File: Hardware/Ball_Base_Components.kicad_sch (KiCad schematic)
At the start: 7 parts, among them U1 TL072

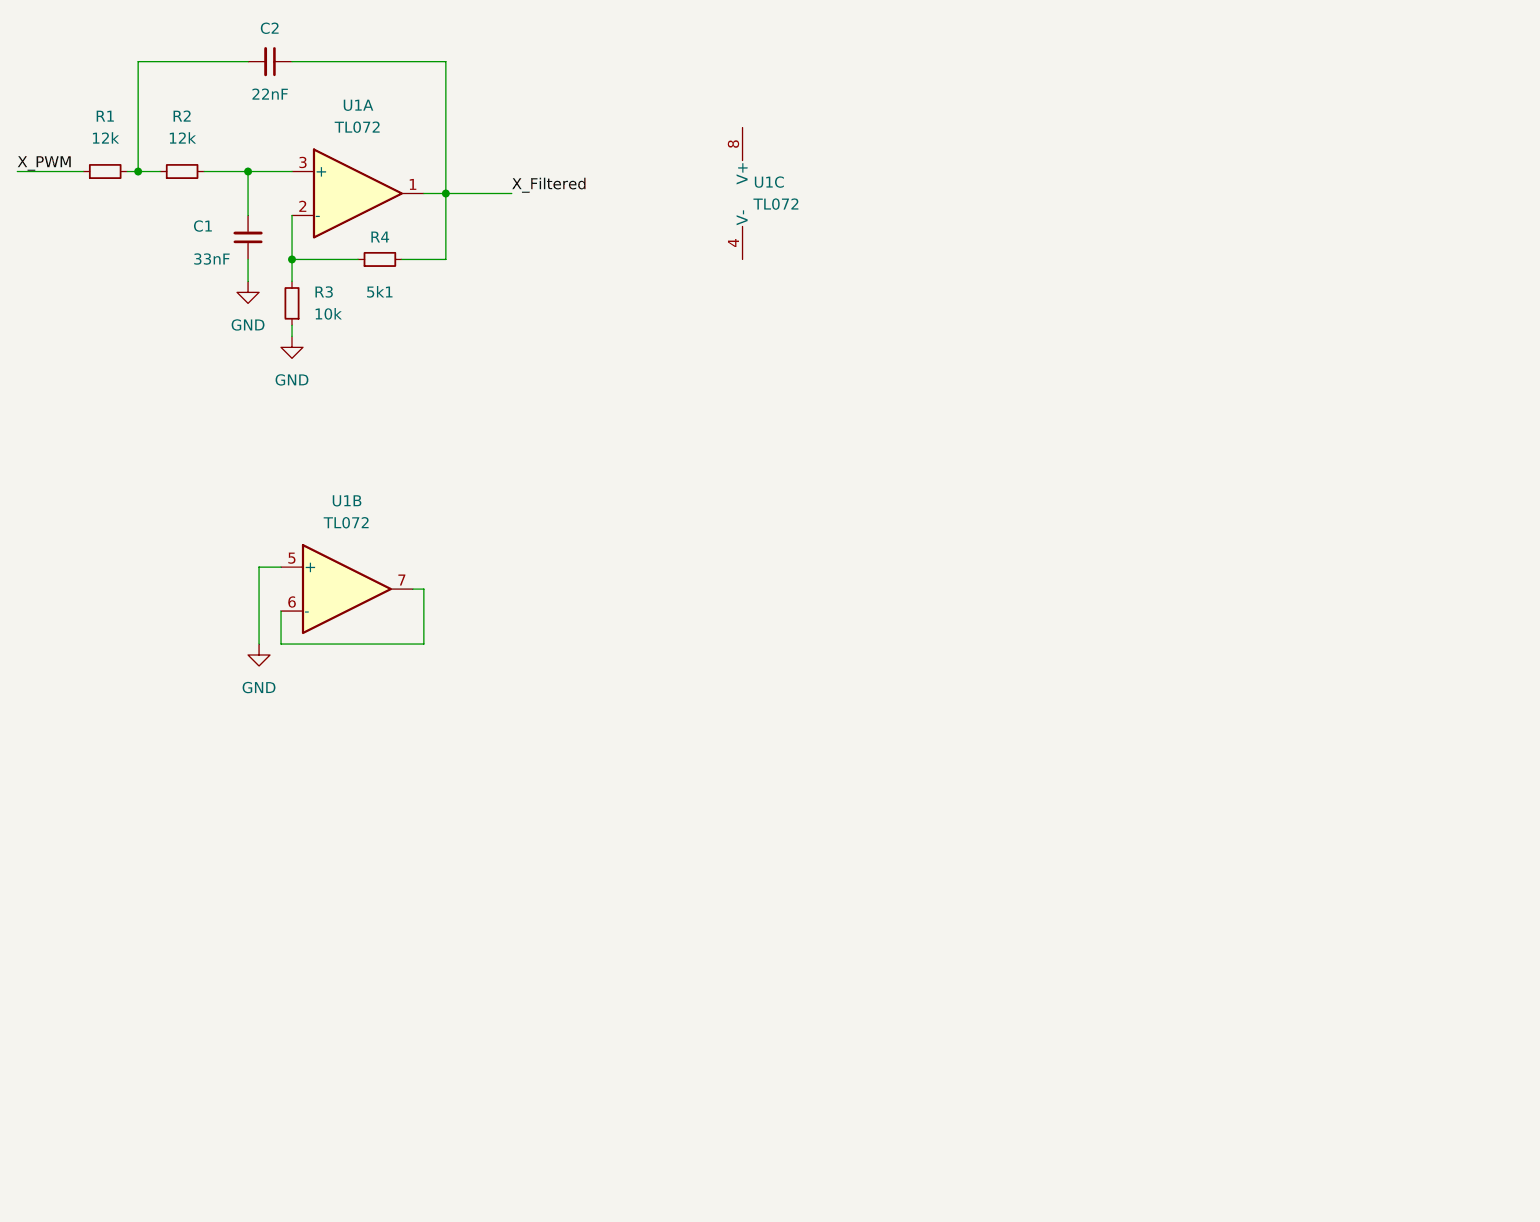
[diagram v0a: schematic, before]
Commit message: Updated base unit to support 3 channels of HID to PWM
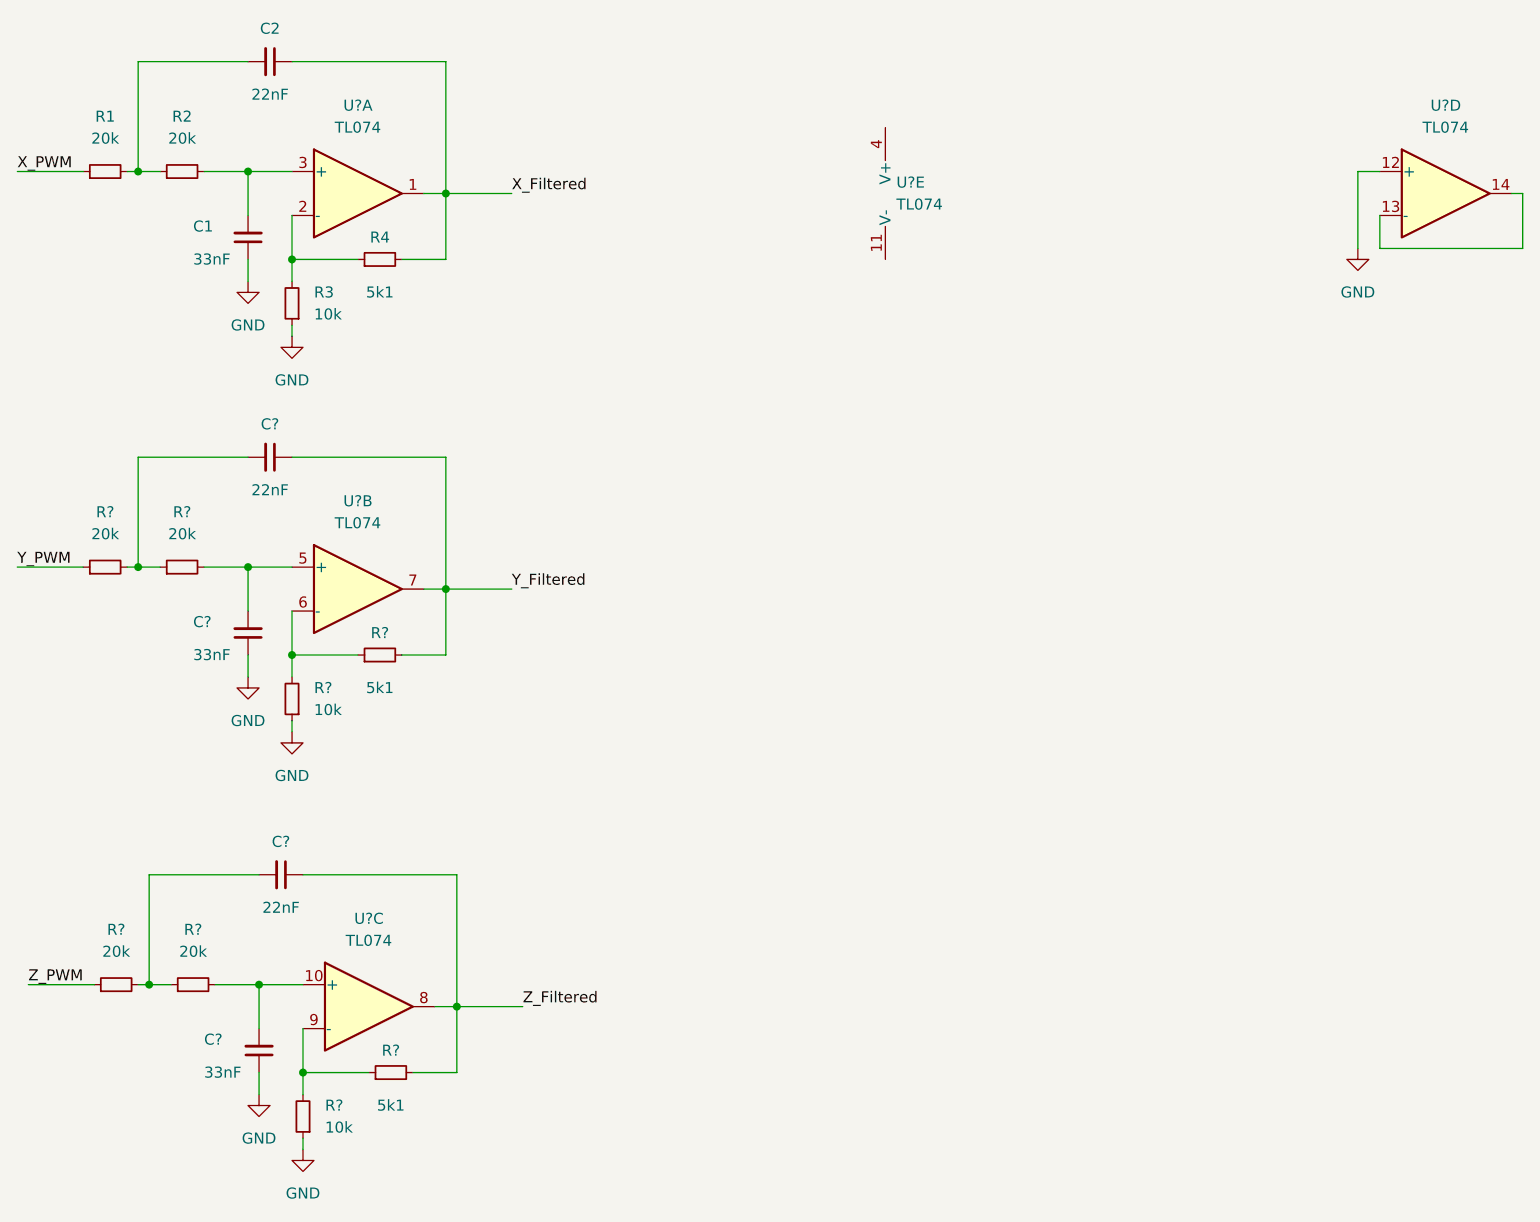
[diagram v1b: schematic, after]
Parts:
- removed U1: TL072, symbol Amplifier_Operational:TL072
- added C? (x2): 33nF, symbol Device:C_Small
- added C? (x2): 22nF, symbol Device:C_Small
- added R? (x4): 20k, symbol Device:R_Small
- added R? (x2): 5k1, symbol Device:R_Small
- added R? (x2): 10k, symbol Device:R_Small
- added U? (x5): TL074, symbol Amplifier_Operational:TL074
- R1, R2: value 12k -> 20k
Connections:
- net GND: now also C?.1, C?.1, R?.1, R?.1, U?.12 (+)
- net X_Filtered: now also U?.1
- net at R3.2, R4.1: now also U?.2 (-)
- net at C1.2, R2.2: now also U?.3 (+)
- new net: C?.2, R?.1, R?.2 (x2)
- new net: C?.2, R?.2, U?.5 (+)
- new net: C?.2, R?.2, U?.10 (+)
- new net: R?.1, R?.2, U?.9 (-)
- new net: U?.13 (-), U?.14
- new net: R?.1, R?.2, U?.6 (-)
- new net Y_Filtered: C?.1, R?.2, U?.7
- new net Y_PWM: R?.1
- new net Z_Filtered: C?.1, R?.2, U?.8
- new net Z_PWM: R?.1

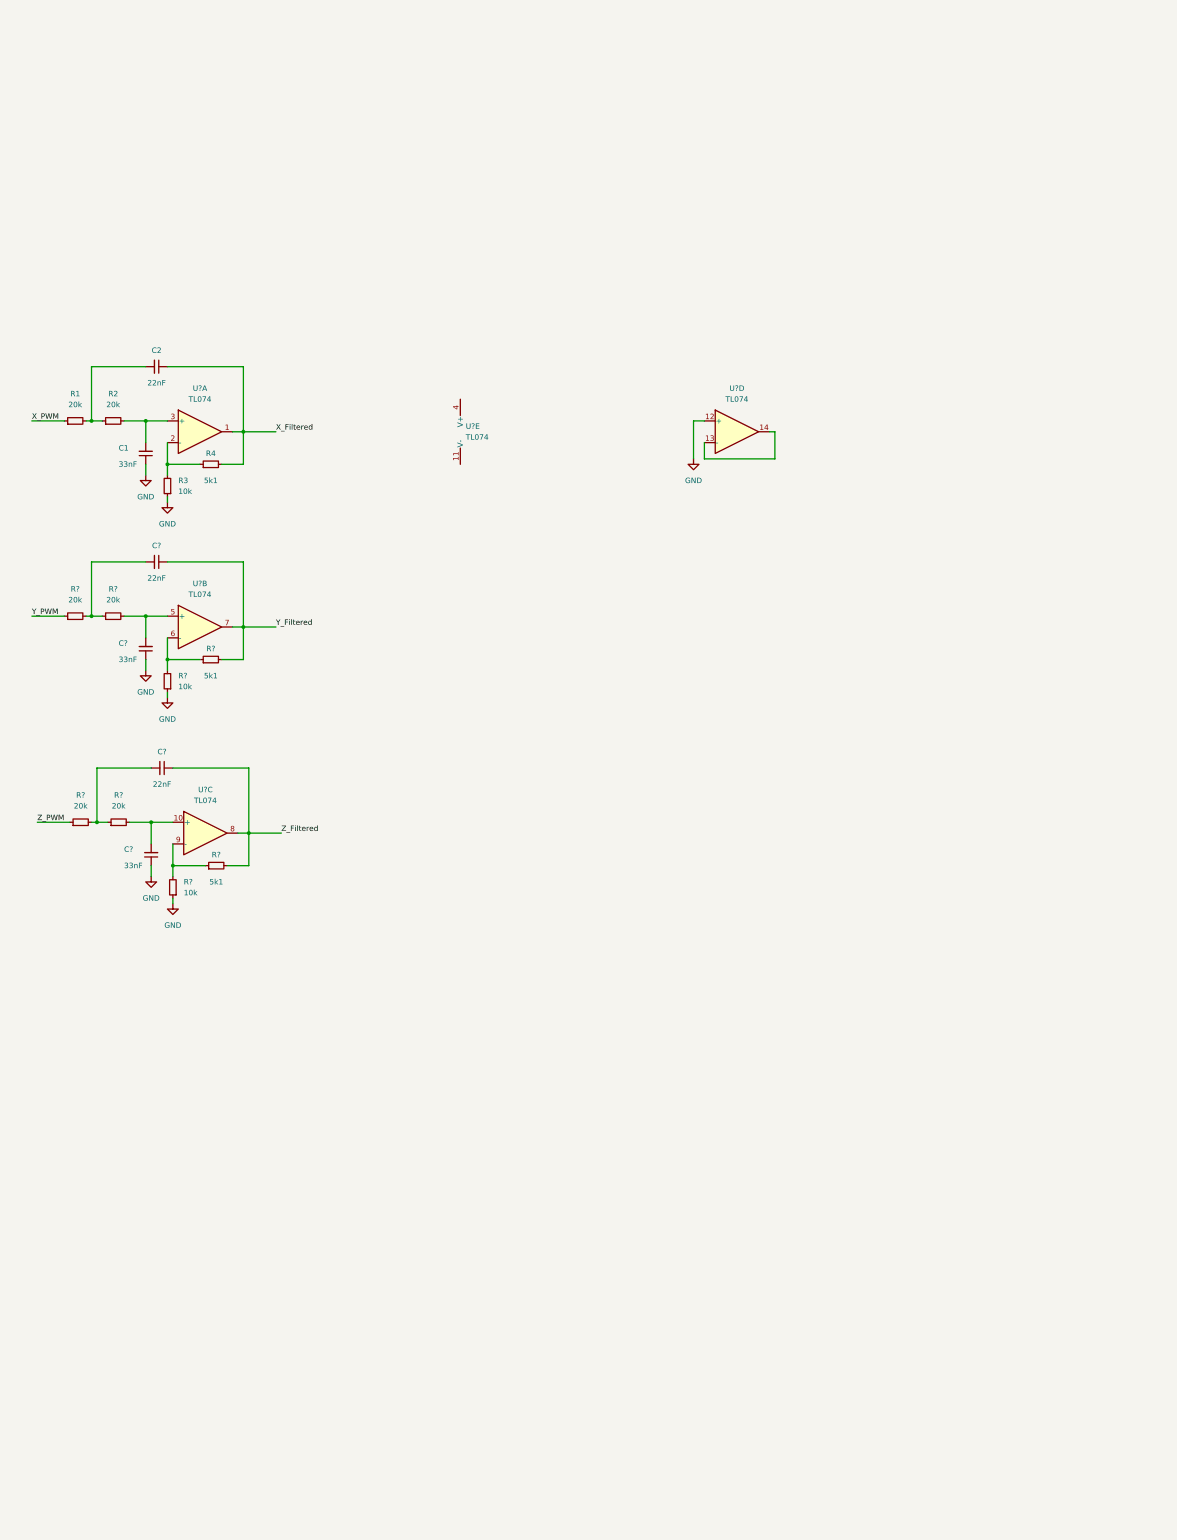
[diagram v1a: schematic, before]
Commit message: Calibration updates; I2C Handling improvements; Started Base Schematic
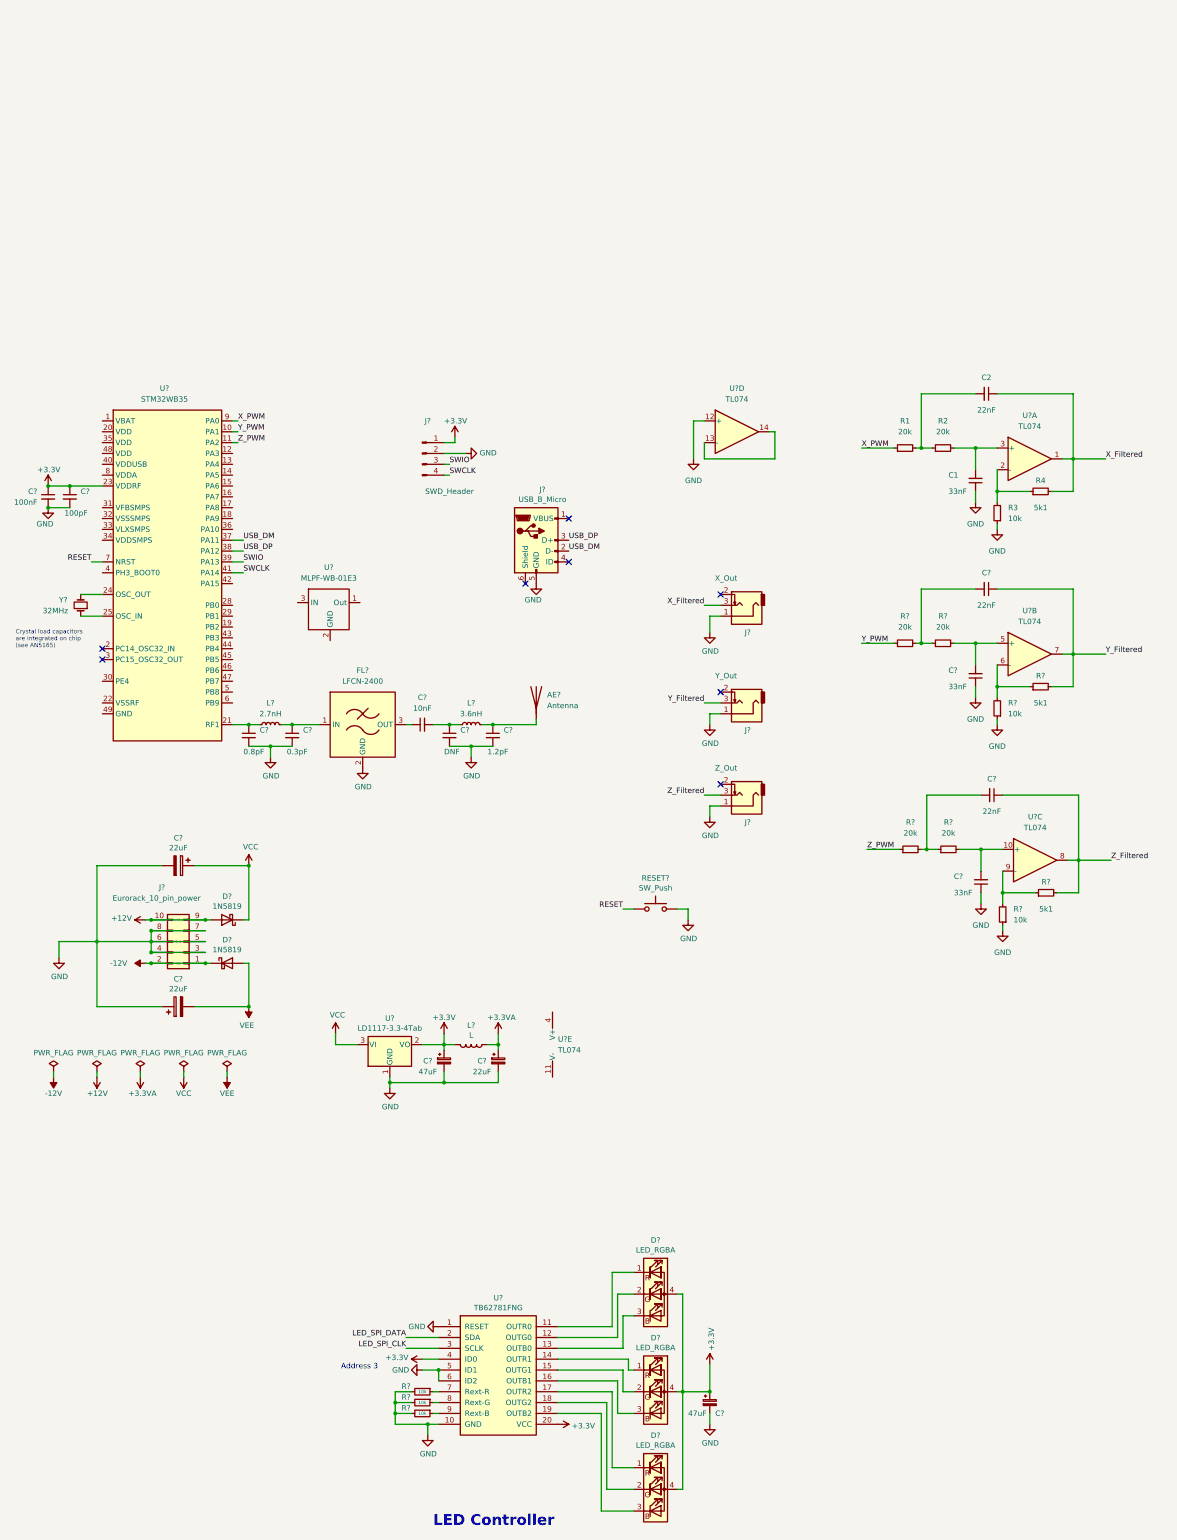
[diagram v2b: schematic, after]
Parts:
- added AE?: Antenna, symbol Device:Antenna
- added C?: 0.8pF, symbol Device:C_Small
- added C? (x2): 47uF, Capacitors_SMD:CP_Elec_5x5.8, symbol Device:CP_Small
- added C?: 22uF, Capacitors_SMD:CP_Elec_4x5.8, symbol Device:CP_Small
- added C?: 10nF, symbol Device:C_Small
- added C?: 22uF, Capacitors_SMD:CP_Elec_4x5.8, symbol Device:CP
- added C?: 100nF, symbol Device:C_Small
- added C?: 1.2pF, symbol Device:C_Small
- added C?: 22uF, Capacitors_SMD:CP_Elec_5x5.8, symbol Device:CP
- added C?: DNF, symbol Device:C_Small
- added C?: 0.3pF, symbol Device:C_Small
- added C?: 100pF, symbol Device:C_Small
- added D? (x3): LED_RGBA, Custom_Footprints:LED_RGB_PLCC4, symbol Device:LED_RGBA
- added D? (x2): 1N5819, Diodes_SMD:D_SOD-123, symbol Diode:1N5819
- added FL?: LFCN-2400, Filter:Filter_Mini-Circuits_FV1206, symbol RF_Filter:LFCN-2400
- added J?: Eurorack_10_pin_power, Custom_Footprints:Eurorack_10_pin_header, symbol Eurorack_Header:Eurorack_10_pin_power
- added J?: USB_B_Micro, Custom_Footprints:USB_Micro-B_Amphenol, symbol Connector:USB_B_Micro
- added J?: X_Out, Custom_Footprints:THONKICONN_hole, symbol thonkiconn:AudioJack2_Ground_Switch
- added J?: Z_Out, Custom_Footprints:THONKICONN_hole, symbol thonkiconn:AudioJack2_Ground_Switch
- added J?: Y_Out, Custom_Footprints:THONKICONN_hole, symbol thonkiconn:AudioJack2_Ground_Switch
- added J?: SWD_Header, Custom_Footprints:SWD_header, symbol Connector:Conn_01x04_Male
- added L?: L, Inductors_SMD:L_0805_HandSoldering, symbol Device:L
- added L?: 3.6nH, symbol Device:L_Small
- added L?: 2.7nH, symbol Device:L_Small
- added R? (x3): 10k, Resistors_SMD:R_0603_HandSoldering, symbol Device:R_Small
- added RESET?: SW_Push, Custom_Footprints:SW_PUSH_6mm_aligned, symbol Switch:SW_Push
- added U?: LD1117-3.3-4Tab, TO_SOT_Packages_SMD:SOT-223-3_TabPin2, symbol LD1117-3.3-4Tab:LD1117-3.3-4Tab
- added U?: STM32WB35, symbol STM32WB35:STM32WB35
- added U?: MLPF-WB-01E3, symbol RF_Filters:MLPF-WB-01E3
- added U?: TB62781FNG, Housings_SSOP:SSOP-20_4.4x6.5mm_Pitch0.65mm, symbol TB62781FNG:TB62781FNG
- added Y?: 32MHz, symbol Device:Crystal_Small
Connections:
- net GND: now also C?.1, C?.2, C?.2, C?.2, C?.2, C?.2, C?.2, C?.2, C?.2, C?.2, C?.2, FL?.2 (GND), FL?.4 (GND), J?.1, J?.1, J?.1, J?.2 (Pin_2), J?.3 (Pin_3), J?.4 (Pin_4), J?.5 (GND), J?.5 (Pin_5), J?.6 (Pin_6), J?.7 (Pin_7), J?.8 (Pin_8), R?.2, R?.2, R?.2, RESET?.2, U?.1 (GND), U?.1 (RESET), U?.10 (GND), U?.5 (ID1), U?.6 (ID2)
- net X_Filtered: now also J?.3
- net X_PWM: now also U?.9 (PA0)
- net Y_Filtered: now also J?.3
- net Y_PWM: now also U?.10 (PA1)
- net Z_Filtered: now also J?.3
- net Z_PWM: now also U?.11 (PA2)
- new net: C?.1, L?.1, U?.21 (RF1)
- new net: R?.1, U?.7 (Rext-R)
- new net: D?.1 (RK), U?.17 (OUTR2)
- new net: D?.2 (GK), U?.18 (OUTG2)
- new net: D?.3 (BK), U?.19 (OUTB2)
- new net: C?.1, FL?.3 (OUT)
- new net: C?.1, C?.2, L?.1
- new net: R?.1, U?.8 (Rext-G)
- new net: AE?.1 (A), C?.1, L?.2
- new net: U?.25 (OSC_IN), Y?.1
- new net: U?.24 (OSC_OUT), Y?.2
- new net: R?.1, U?.9 (Rext-B)
- new net: C?.1, FL?.1 (IN), L?.2
- new net: D?.1 (RK), U?.11 (OUTR0)
- new net: D?.2 (GK), U?.12 (OUTG0)
- new net: D?.3 (BK), U?.13 (OUTB0)
- new net: D?.1 (RK), U?.14 (OUTR1)
- new net: D?.2 (GK), U?.15 (OUTG1)
- new net: D?.3 (BK), U?.16 (OUTB1)
- new net: U?.26 (AT0), U?.27 (AT1)
- new net: U?.2 (GND), U?.4 (GND), U?.5 (GND), U?.6 (GND)
- new net +12V: D?.2 (A), J?.10 (Pin_10), J?.9 (Pin_9)
- new net +3.3VA: C?.1, L?.1
- new net +3V3: C?.1, C?.1, C?.1, C?.1, D?.4 (A), D?.4 (A), D?.4 (A), J?.1 (Pin_1), L?.2, U?.2 (VO), U?.20 (VCC), U?.23 (VDDRF), U?.4 (ID0)
- new net -12V: D?.1 (K), J?.1 (Pin_1), J?.2 (Pin_2)
- new net LED_SPI_CLK: U?.3 (SCLK)
- new net LED_SPI_DATA: U?.2 (SDA)
- new net RESET: RESET?.1, U?.7 (NRST)
- new net SWCLK: J?.4 (Pin_4), U?.41 (PA14)
- new net SWIO: J?.3 (Pin_3), U?.39 (PA13)
- new net USB_DM: J?.2 (D-), U?.37 (PA11)
- new net USB_DP: J?.3 (D+), U?.38 (PA12)
- new net VCC: C?.1, D?.1 (K), U?.3 (VI)
- new net VEE: C?.2, D?.2 (A)
- no-connect marks 0 -> 8
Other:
- note added: "Address 3"
- note added: "Crystal load capacitors are integrated on chip (see AN5165)"
- note added: "LED Controller"
- moved on the sheet: C1, C2, C?, R1, R2, R3, R4, R?, U?A, U?B, U?C, U?E
